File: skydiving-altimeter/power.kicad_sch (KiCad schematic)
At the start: 8 parts, among them U4 RP400N501A-TR-FE, U5 LDL1117S33R

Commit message: Finished reroute
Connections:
- net 5V_OUT: now also C15.1
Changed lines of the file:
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@@
   (junction (at 151.13 72.39) (diameter 0) (color 0 0 0 0)
+  )
+  (junction (at 160.02 85.09) (diameter 0) (color 0 0 0 0)
   )
   (junction (at 151.13 85.09) (diameter 0) (color 0 0 0 0)
@@
     (stroke (width 0) (type default) (color 0 0 0 0))
   )
+  (wire (pts (xy 160.02 85.09) (xy 151.13 85.09))
+    (stroke (width 0) (type default) (color 0 0 0 0))
+  )
   (wire (pts (xy 151.13 88.9) (xy 144.78 88.9))
     (stroke (width 0) (type default) (color 0 0 0 0))
@@
     (stroke (width 0) (type default) (color 0 0 0 0))
   )
-  (wire (pts (xy 165.1 85.09) (xy 151.13 85.09))
+  (wire (pts (xy 165.1 85.09) (xy 160.02 85.09))
     (stroke (width 0) (type default) (color 0 0 0 0))
   )

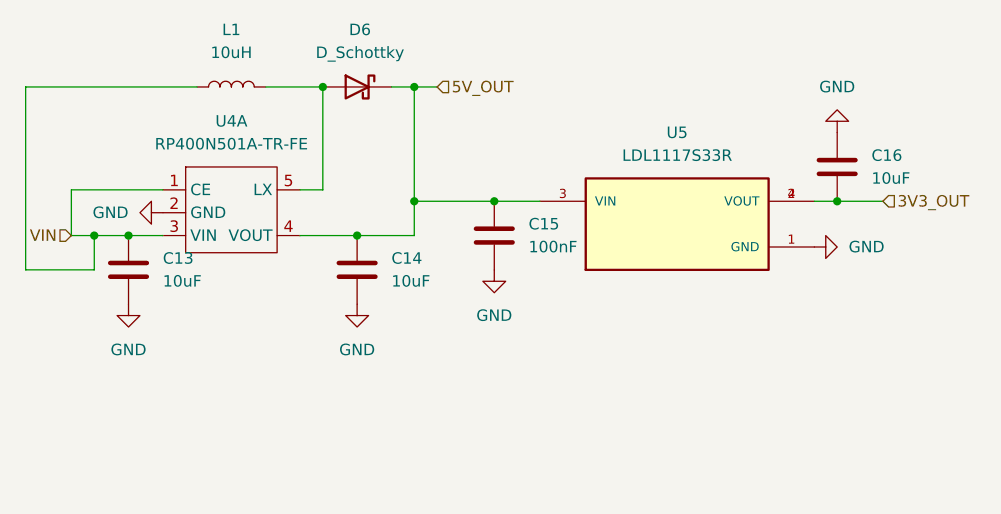
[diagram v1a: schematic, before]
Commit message: Began adding 10 ohm current limiting resistors
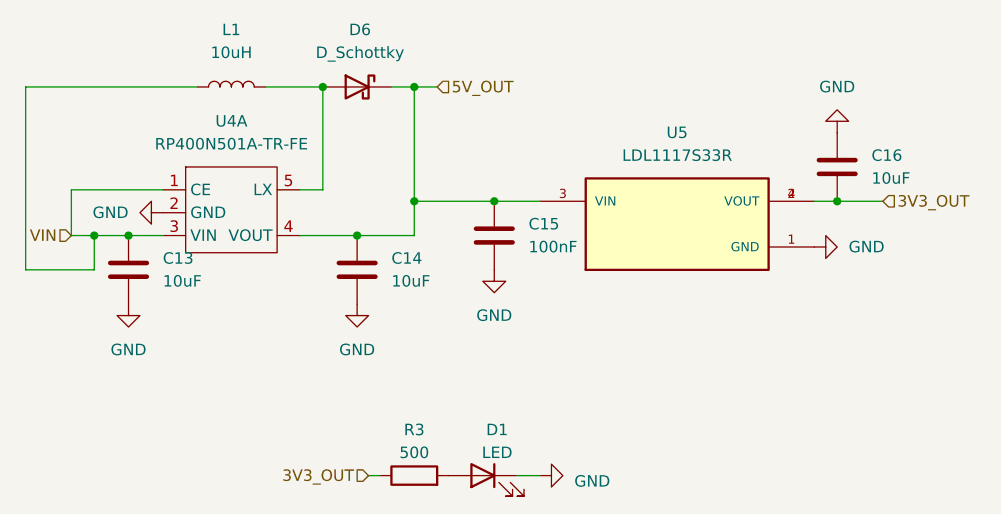
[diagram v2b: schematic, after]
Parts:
- added D1: LED, Diode_SMD:D_0603_1608Metric, symbol Device:LED
- added R3: 500, Resistor_SMD:R_0805_2012Metric, symbol Device:R
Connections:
- net 3V3_OUT: now also R3.1
- net GND: now also D1.1 (K)
- new net: D1.2 (A), R3.2

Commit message: Switched most components to 0402
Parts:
- C13, C14, C15, C16: footprint Capacitor_SMD:C_0805_2012Metric -> Capacitor_SMD:C_0402_1005Metric
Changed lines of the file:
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@@
       (effects (font (size 1.27 1.27)) (justify left))
     )
-    (property "Footprint" "Capacitor_SMD:C_0805_2012Metric" (at 120.3452 96.52 0)
+    (property "Footprint" "Capacitor_SMD:C_0402_1005Metric" (at 120.3452 96.52 0)
       (effects (font (size 1.27 1.27)) hide)
     )
@@
       (effects (font (size 1.27 1.27)) (justify left))
     )
-    (property "Footprint" "Capacitor_SMD:C_0805_2012Metric" (at 145.7452 96.52 0)
+    (property "Footprint" "Capacitor_SMD:C_0402_1005Metric" (at 145.7452 96.52 0)
       (effects (font (size 1.27 1.27)) hide)
     )
@@
       (effects (font (size 1.27 1.27)) (justify left))
     )
-    (property "Footprint" "Capacitor_SMD:C_0805_2012Metric" (at 199.0852 85.09 0)
+    (property "Footprint" "Capacitor_SMD:C_0402_1005Metric" (at 199.0852 85.09 0)
       (effects (font (size 1.27 1.27)) hide)
     )
@@
       (effects (font (size 1.27 1.27)) (justify left))
     )
-    (property "Footprint" "Capacitor_SMD:C_0805_2012Metric" (at 160.9852 92.71 0)
-      (effects (font (size 1.27 1.27)) hide)
-    )
+    (property "Footprint" "Capacitor_SMD:C_0402_1005Metric" (at 160.9852 92.71 0)
+      (effects (font (size 1.27 1.27)) hide)
+    )
